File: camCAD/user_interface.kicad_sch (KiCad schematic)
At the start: 0 parts

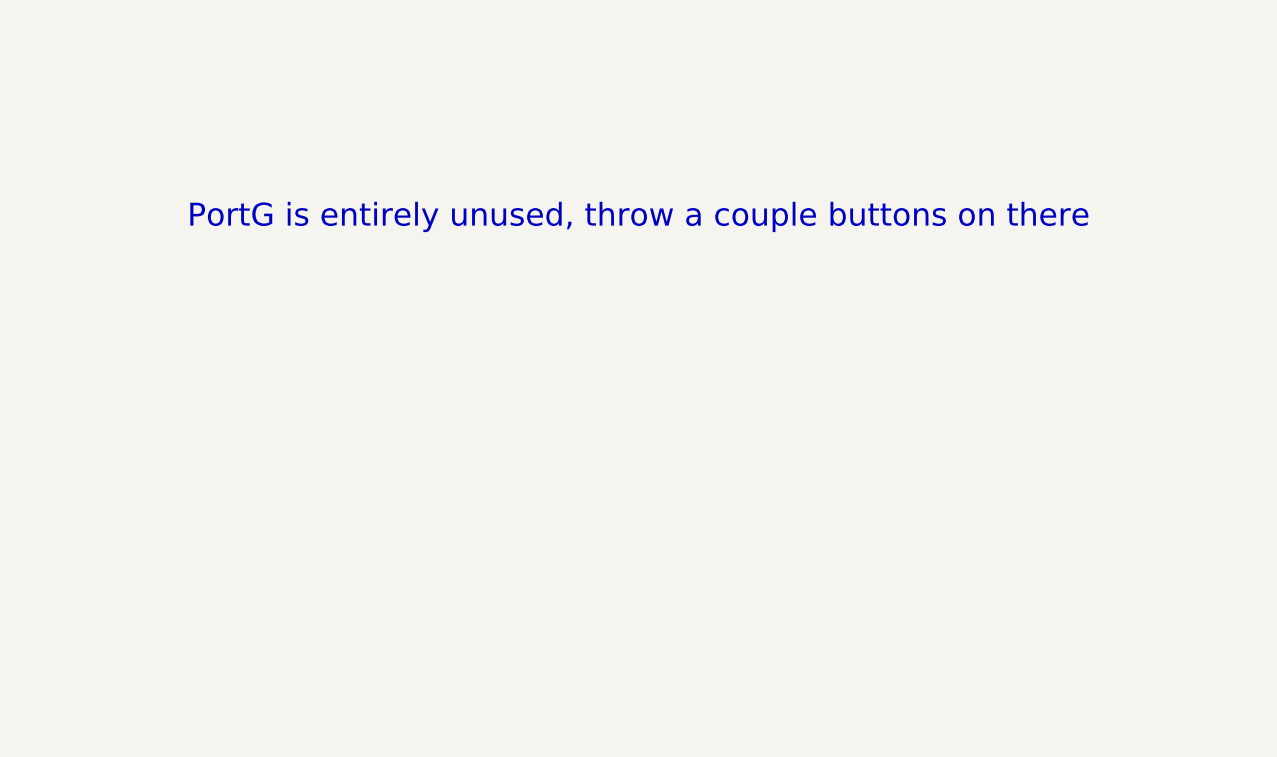
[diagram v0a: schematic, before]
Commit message: Added user interface schematic and updated "camCAD/README.md"
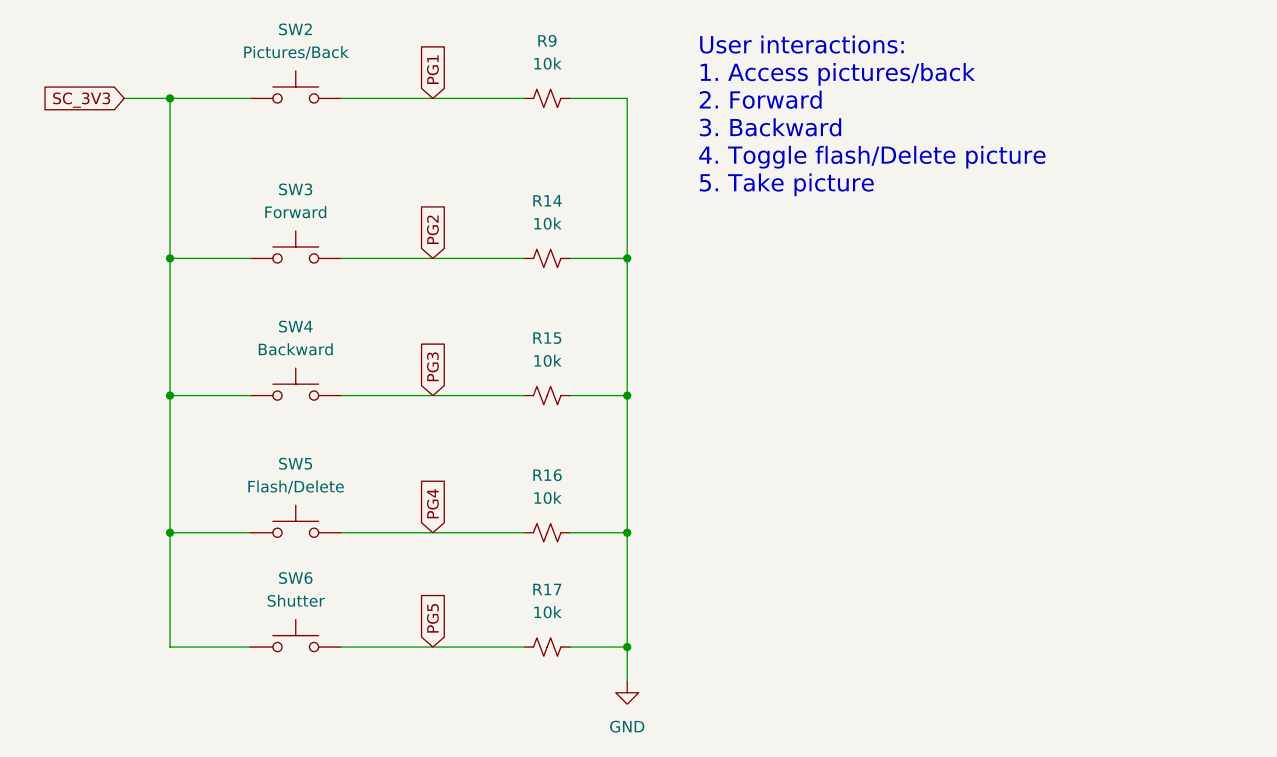
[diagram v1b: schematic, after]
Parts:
- added R14, R15, R16, R17, R9: 10k, Resistor_SMD:R_0402_1005Metric, symbol Device:R_Small_US
- added SW2: Pictures/Back, 1_Switches:SW_SKRPABE010, symbol Switch:SW_Push
- added SW3: Forward, 1_Switches:SW_SKRPABE010, symbol Switch:SW_Push
- added SW4: Backward, 1_Switches:SW_SKRPABE010, symbol Switch:SW_Push
- added SW5: Flash/Delete, 1_Switches:SW_SKRPABE010, symbol Switch:SW_Push
- added SW6: Shutter, 1_Switches:SW_SKRPABE010, symbol Switch:SW_Push
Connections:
- new net GND: R14.2, R15.2, R16.2, R17.2, R9.2
- new net PG1: R9.1, SW2.2
- new net PG2: R14.1, SW3.2
- new net PG3: R15.1, SW4.2
- new net PG4: R16.1, SW5.2
- new net PG5: R17.1, SW6.2
- new net SC_3V3: SW2.1, SW3.1, SW4.1, SW5.1, SW6.1
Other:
- note added: "User interactions: 1. Access pictures/back 2. Forward 3. Backward 4. Toggle flash/Delete picture 5. Take picture"
- note removed: "PortG is entirely unused, throw a couple buttons on there"
- title: (none) -> User Interface/Camera Controls
